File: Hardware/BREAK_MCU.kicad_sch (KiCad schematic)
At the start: 57 parts, among them J24 WAFER-GH1.25-4PLB, Q14 NCE01ND03S, Q16 NCE01ND03S, U28 PY32F002BF15U, U29 EG2104, U30 ZX-HY2.0-2PWT, U31 RT9193-33GB-MS, U32 EG2104, U33 ZX-HY2.0-2PWT, U35 RS622XTDE8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

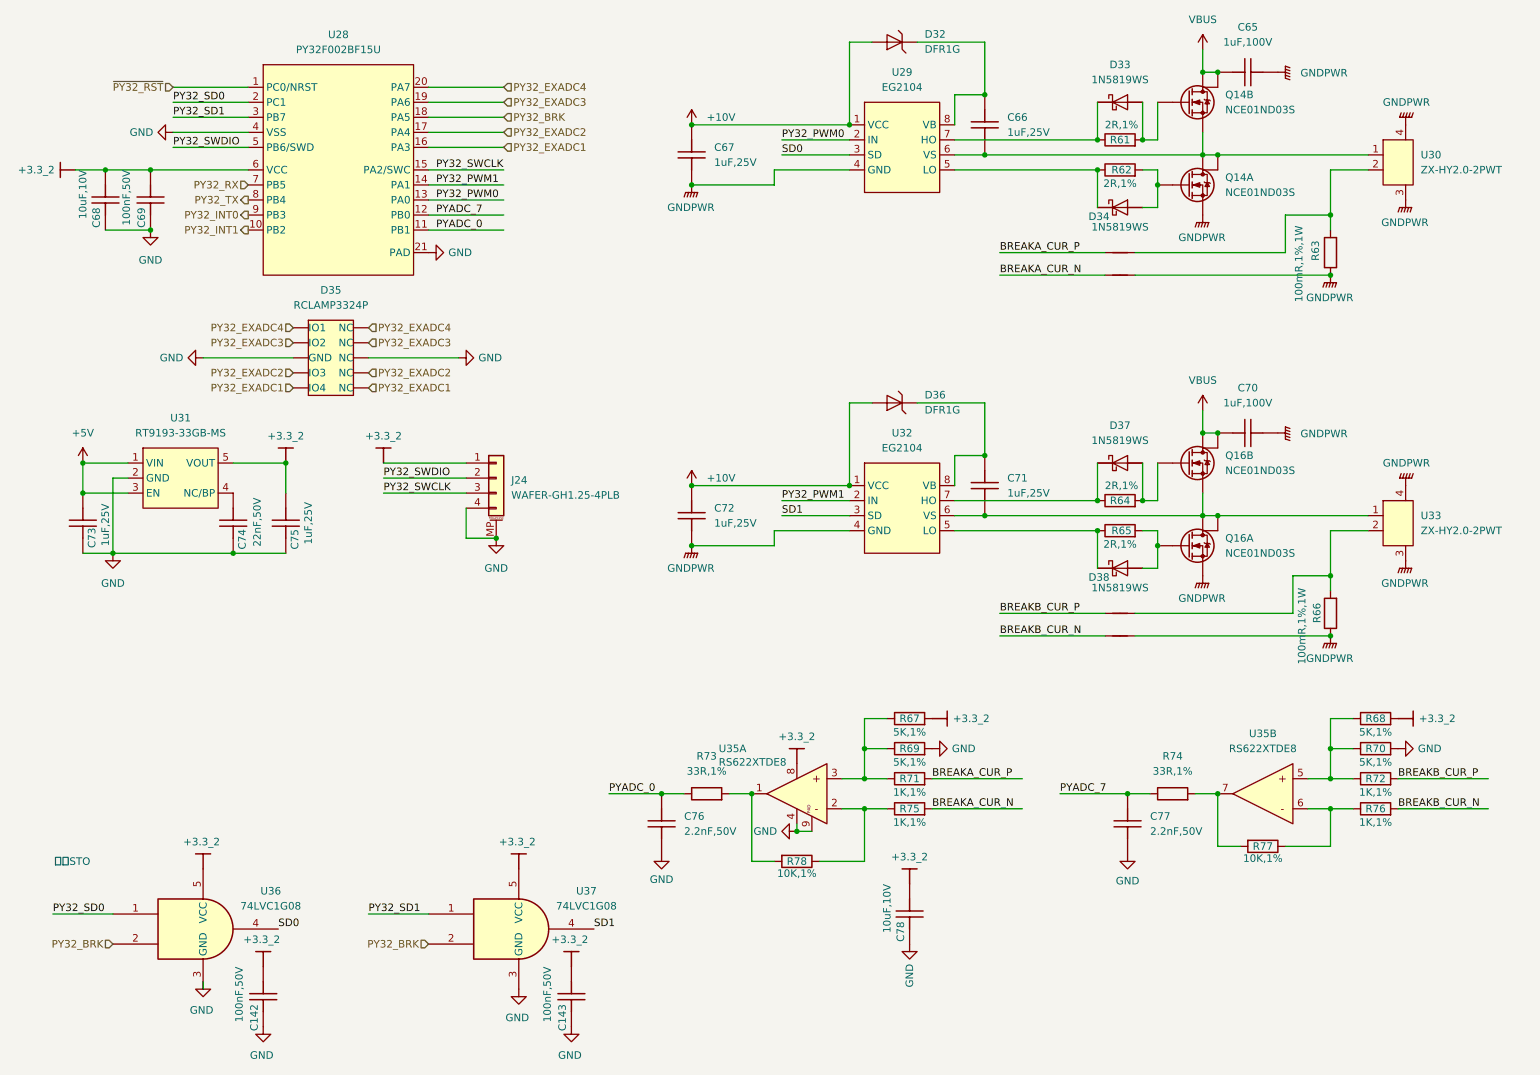
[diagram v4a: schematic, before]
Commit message: 修改PCB，上传py32抱闸驱动代码，上传HPM board
调整抱闸驱动栅极电阻
急停光耦增加上拉电阻和滤波电路
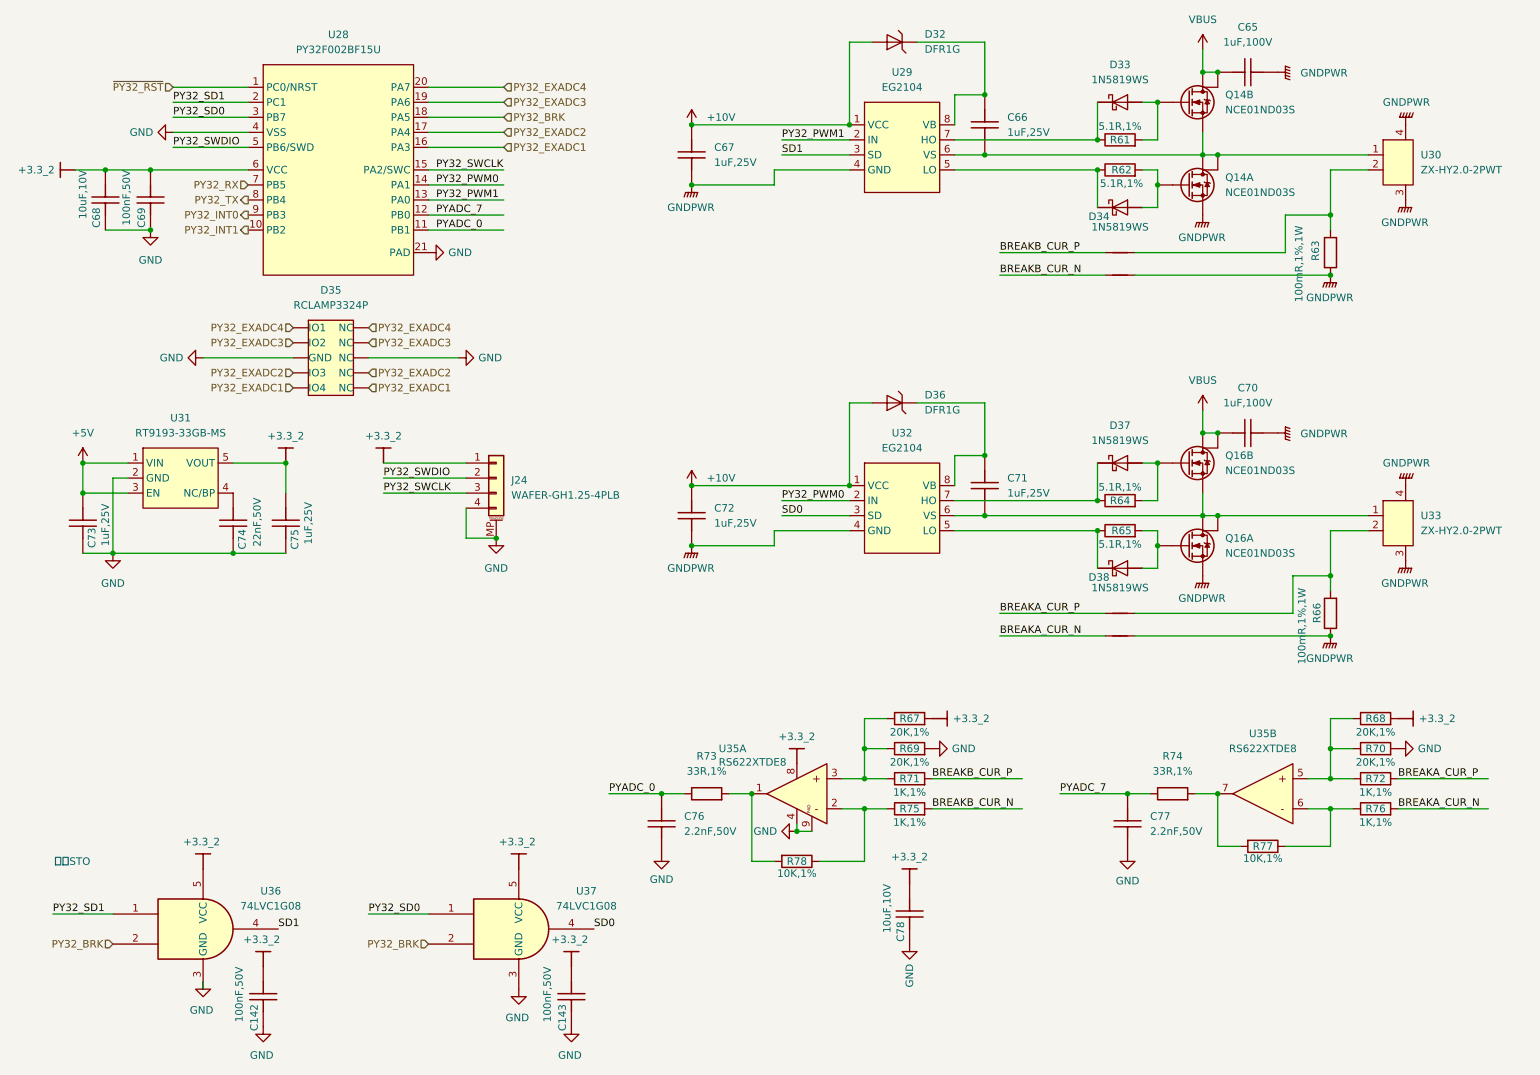
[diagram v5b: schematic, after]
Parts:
- R61, R62, R64, R65: value 2R,1% -> 5.1R,1%; symbol HPM6280Foc:0402WGF200KTCE -> HPM6280Foc:0402WGF510KTCE; 立创编号 C270630 -> C25128
- R67, R68, R69, R70: value 5K,1% -> 20K,1%; symbol HPM6280Foc:RC0402FR-075KL -> HPM6280Foc:0402WGF2002TCE; 立创编号 C477765 -> C25765
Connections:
- net BREAKA_CUR_N: now also NT20.1, R76.2; no longer NT18.1, R75.2
- net BREAKA_CUR_P: now also NT19.1, R72.2; no longer NT17.1, R71.2
- net BREAKB_CUR_N: now also NT18.1, R75.2; no longer NT20.1, R76.2
- net BREAKB_CUR_P: now also NT17.1, R71.2; no longer NT19.1, R72.2
- net PY32_PWM0: now also U28.14 (PA1), U32.2 (IN); no longer U28.13 (PA0), U29.2 (IN)
- net PY32_PWM1: now also U28.13 (PA0), U29.2 (IN); no longer U28.14 (PA1), U32.2 (IN)
- net PY32_SD0: now also U28.3 (PB7), U37.1; no longer U28.2 (PC1), U36.1
- net PY32_SD1: now also U28.2 (PC1), U36.1; no longer U28.3 (PB7), U37.1
- net SD0: now also U32.3 (SD), U37.4; no longer U29.3 (SD), U36.4
- net SD1: now also U29.3 (SD), U36.4; no longer U32.3 (SD), U37.4

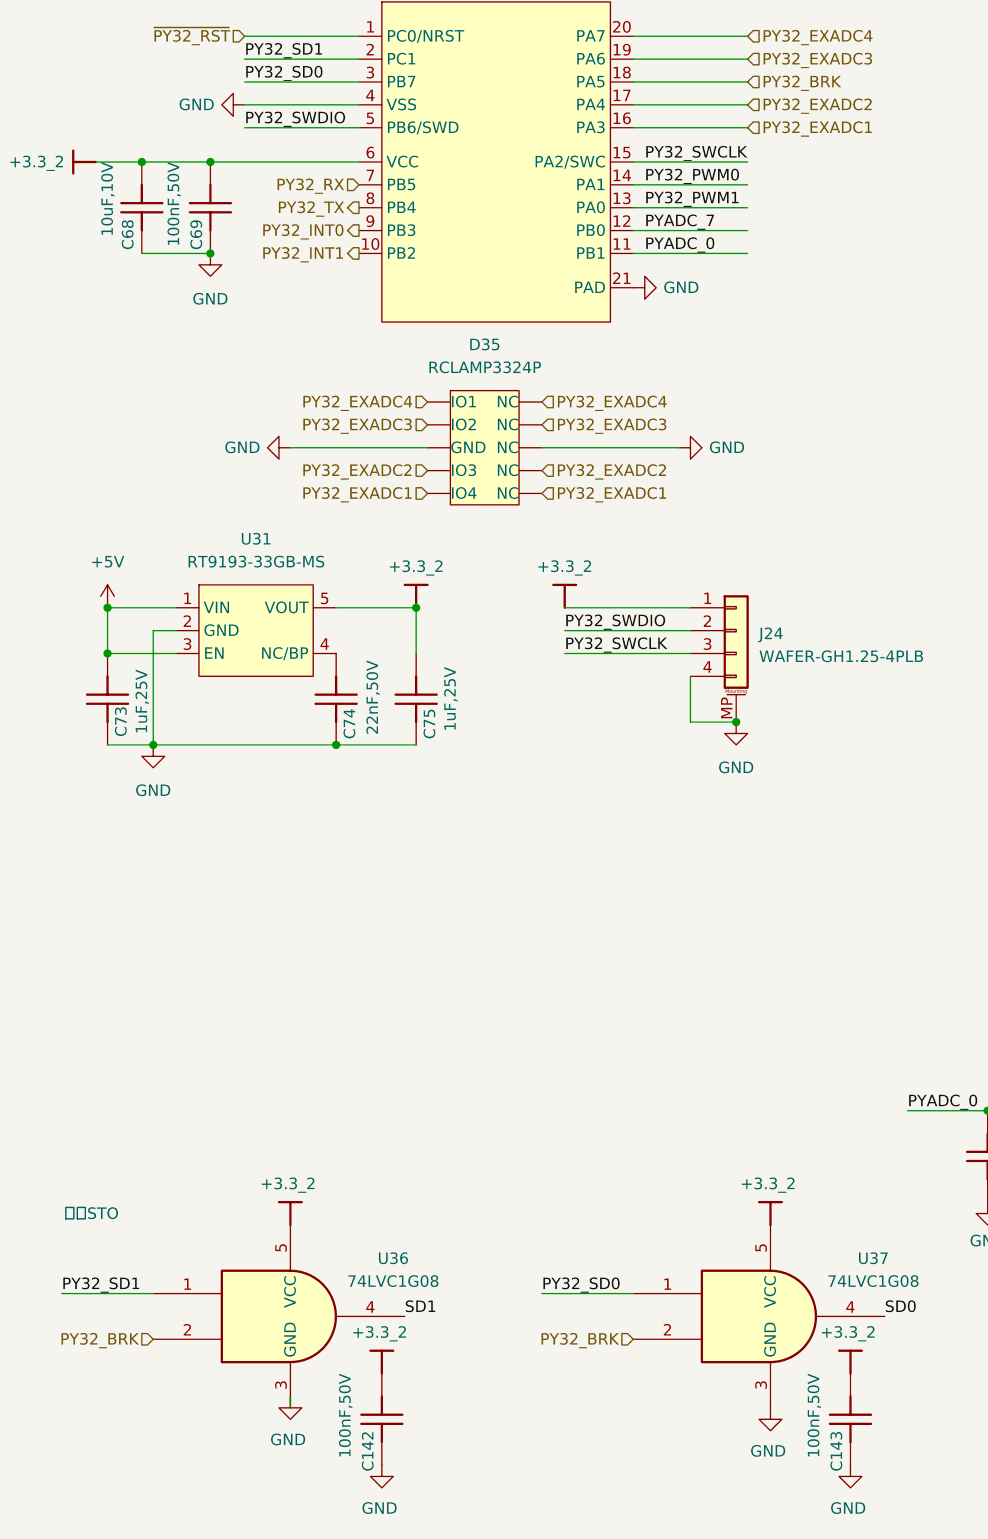
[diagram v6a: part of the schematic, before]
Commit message: PCB优化，修改母线电流采样电阻为2mR，栅极驱动器输入pwm增加滤波防干扰，其他少量优化
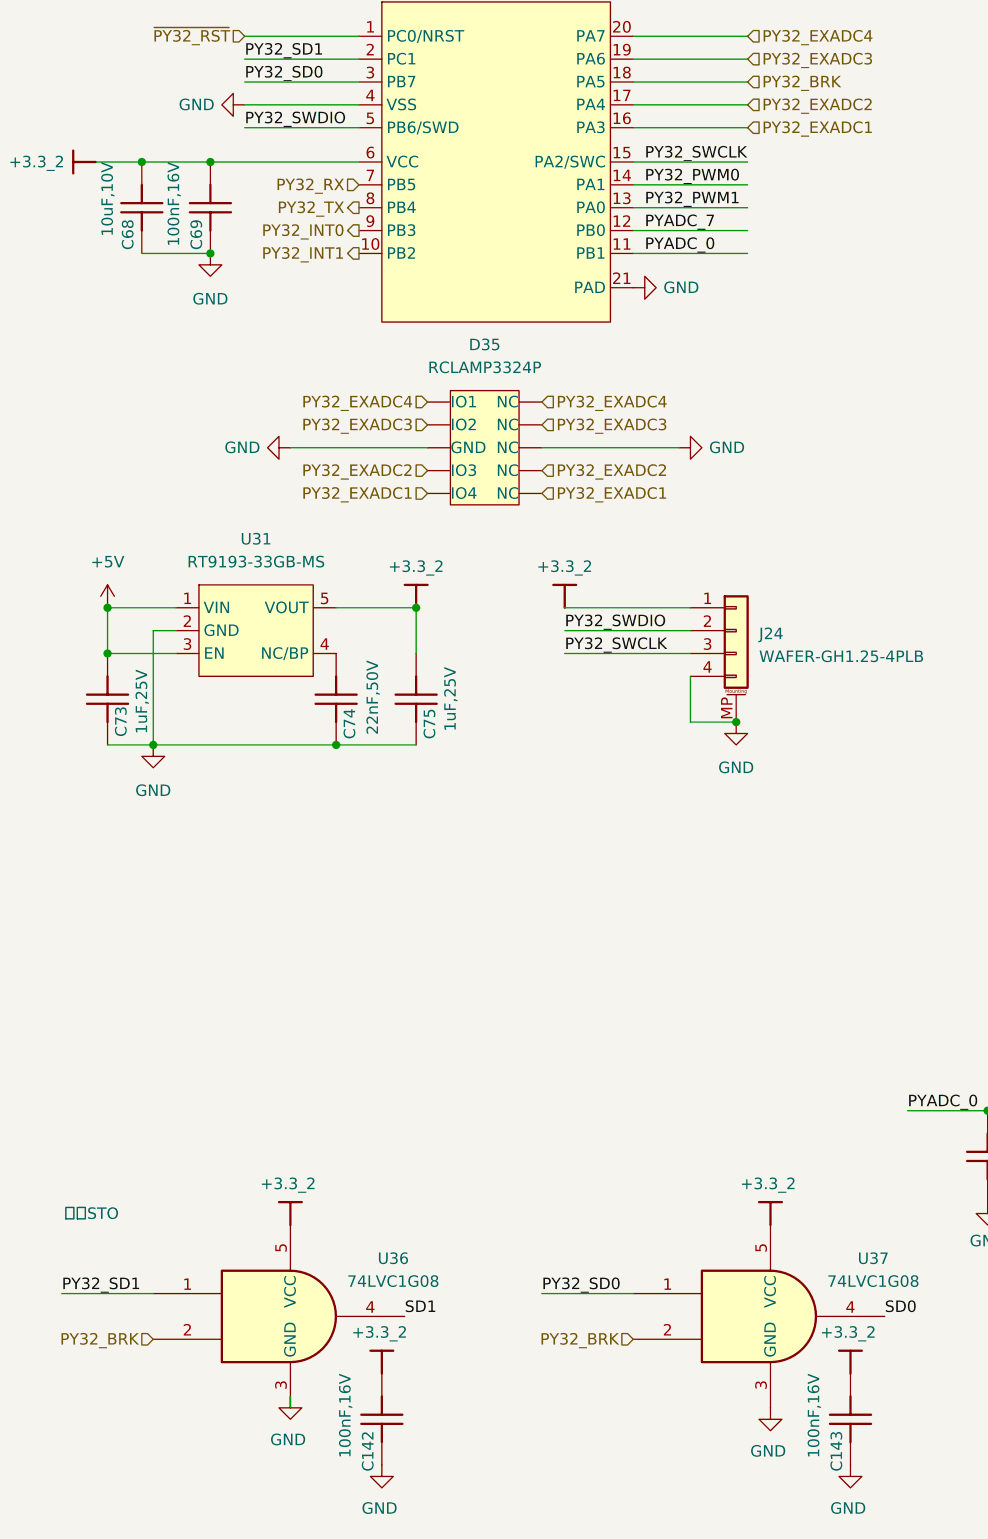
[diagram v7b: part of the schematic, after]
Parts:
- C142, C143, C69: value 100nF,50V -> 100nF,16V
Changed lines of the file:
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@@
 			)
 		)
-		(property "Value" "100nF,50V"
+		(property "Value" "100nF,16V"
 			(at 32.766 44.45 0)
 			(effects
@@
 			)
 		)
-		(property "Value" "100nF,50V"
+		(property "Value" "100nF,16V"
 			(at 103.886 179.07 0)
 			(effects
@@
 			)
 		)
-		(property "Value" "100nF,50V"
+		(property "Value" "100nF,16V"
 			(at 51.816 179.07 0)
 			(effects
